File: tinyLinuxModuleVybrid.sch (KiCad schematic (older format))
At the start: 53 parts, among them M1 SCREW, M2 SCREW, M3 SCREW, M4 SCREW, M5 SCREW, M6 SCREW, M7 SCREW, M8 SCREW, Q1 2N7002BKT, Q2 2N7002BKT, Q3 2N7002BKT, X1 CONN_02x50, X10 MagJack100, X11 MICROSD, X12 CONN_01x03, X2 CONN_02x50, X3 USB4DUAL, X4 CONN_02x25, X5 ARM_JTAG_10, X6 USB4DUAL, X7 CONN_02x20, X8 CONN_02x14

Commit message: NEO_modifiziert
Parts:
- removed V1: 5V, Passives:V0805N, symbol V
- removed X12: CONN_01x03, Connector:PinHD-90-2.54-01x03-THT, symbol CONN_01X03
- removed X3, X6: USB4DUAL, Connector:USB4DUAL_A, symbol USB4DUAL
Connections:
- wire segments 429 -> 383
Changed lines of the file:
@@
 PTB5
-$Comp
-L GND #PWR062
-U 1 1 5601F6AC
-P 3900 4600
-F 0 "#PWR062" H 3900 4350 50  0001 C CNN
-F 1 "GND" H 3900 4450 50  0000 C CNN
-F 2 "" H 3900 4600 60  0000 C CNN
-F 3 "" H 3900 4600 60  0000 C CNN
-	1    3900 4600
-	1    0    0    -1
-$EndComp
 $Comp
 L GND #PWR063
@@
 $EndSheet
 $Comp
-L USB4DUAL X3
-U 1 1 56289EB9
-P 4550 2300
-F 0 "X3" H 4400 2900 50  0000 C CNN
-F 1 "USB4DUAL" V 4750 2350 50  0000 C CNN
-F 2 "Connector:USB4DUAL_A" H 4400 2550 60  0001 C CNN
-F 3 "" H 4400 2550 60  0000 C CNN
-	1    4550 2300
-	1    0    0    -1
-$EndComp
-$Comp
-L USB4DUAL X6
-U 1 1 56289FBC
-P 4550 3550
-F 0 "X6" H 4400 4150 50  0000 C CNN
-F 1 "USB4DUAL" V 4750 3600 50  0000 C CNN
-F 2 "Connector:USB4DUAL_A" H 4400 3800 60  0001 C CNN
-F 3 "" H 4400 3800 60  0000 C CNN
-	1    4550 3550
-	1    0    0    -1
-$EndComp
-$Comp
 L CONN_02X20 X7
 U 1 1 5628A750
@@
 USB
 $Comp
-L V V1
-U 1 1 56359904
-P 4100 4300
-F 0 "V1" V 4180 4300 50  0000 C CNN
-F 1 "5V" V 4020 4300 50  0000 C CNN
-F 2 "Passives:V0805N" V 4030 4300 30  0001 C CNN
-F 3 "" H 4100 4300 30  0000 C CNN
-	1    4100 4300
-	1    0    0    -1
-$EndComp
-$Comp
 L GND #PWR064
 U 1 1 56360C40
@@
 	2850 1600 5000 1600
 Wire Wire Line
-	3550 2600 2850 2600
-Wire Wire Line
-	2850 2500 3600 2500
-Wire Wire Line
-	3650 2400 2850 2400
-Wire Wire Line
-	2850 2300 3700 2300
-Connection ~ 3900 2600
-Wire Wire Line
-	4200 2100 3900 2100
-Connection ~ 3900 3350
-Wire Wire Line
-	4200 2600 3900 2600
-Connection ~ 3900 3850
-Wire Wire Line
-	3900 3350 4200 3350
-Connection ~ 3900 4550
-Wire Wire Line
-	3900 3850 4200 3850
-Wire Wire Line
-	3900 2100 3900 4600
-Wire Wire Line
-	4100 4550 3900 4550
-Wire Wire Line
-	4100 4500 4100 4550
-Connection ~ 4100 4050
-Wire Wire Line
-	4200 4050 4100 4050
-Wire Wire Line
-	4100 2800 4100 4100
-Wire Wire Line
-	4200 2800 4100 2800
-Connection ~ 4150 3050
-Wire Wire Line
-	4150 3550 4200 3550
-Connection ~ 4150 2300
-Wire Wire Line
-	4150 3050 4200 3050
-Connection ~ 4150 1800
-Wire Wire Line
-	4150 1800 4150 3550
-Wire Wire Line
-	4200 2300 4150 2300
-Wire Wire Line
 	1250 2700 600  2700
 Wire Wire Line
@@
 Wire Wire Line
 	2200 6800 2200 6750
-$Comp
-L CONN_01X03 X12
-U 1 1 563D7E2E
-P 8000 900
-F 0 "X12" H 8000 1100 50  0000 C CNN
-F 1 "CONN_01x03" V 8100 900 50  0000 C CNN
-F 2 "Connector:PinHD-90-2.54-01x03-THT" H 8000 900 60  0001 C CNN
-F 3 "" H 8000 900 60  0000 C CNN
-	1    8000 900
-	1    0    0    -1
-$EndComp
-Wire Wire Line
-	2850 800  7800 800
-Wire Wire Line
-	2850 900  7800 900
-$Comp
-L GND #PWR0100
-U 1 1 563D890F
-P 7750 1050
-F 0 "#PWR0100" H 7750 800 50  0001 C CNN
-F 1 "GND" H 7750 900 50  0000 C CNN
-F 2 "" H 7750 1050 60  0000 C CNN
-F 3 "" H 7750 1050 60  0000 C CNN
-	1    7750 1050
-	1    0    0    -1
-$EndComp
-Wire Wire Line
-	7800 1000 7750 1000
-Wire Wire Line
-	7750 1000 7750 1050
 $Comp
 L GND #PWR0101
@@
 	1    0    0    -1
 $EndComp
-Wire Wire Line
-	3700 2300 3700 3750
-Wire Wire Line
-	3650 3650 3650 2400
-Wire Wire Line
-	3600 2500 3600 3250
-Wire Wire Line
-	3550 3150 3550 2600
-Wire Wire Line
-	3750 2200 2850 2200
-Wire Wire Line
-	3750 1900 3750 2200
-Wire Wire Line
-	2850 2100 3700 2100
-Wire Wire Line
-	3700 2100 3700 2000
-Wire Wire Line
-	2850 2000 3400 2000
-Wire Wire Line
-	3400 2000 3400 2250
-Wire Wire Line
-	3400 2250 3750 2250
-Wire Wire Line
-	3750 2250 3750 2400
-Wire Wire Line
-	2850 1900 3500 1900
-Wire Wire Line
-	3500 1900 3500 2150
-Wire Wire Line
-	3500 2150 3800 2150
-Wire Wire Line
-	3800 2150 3800 2500
 $Comp
 L R R34
@@
 Wire Wire Line
 	3850 5200 3550 5200
-Wire Wire Line
-	3800 2500 4200 2500
-Wire Wire Line
-	3750 2400 4200 2400
-Wire Wire Line
-	4200 1900 3750 1900
-Wire Wire Line
-	3700 2000 4200 2000
-Wire Wire Line
-	3600 3250 4200 3250
-Wire Wire Line
-	3700 3750 4200 3750
-Wire Wire Line
-	4200 3650 3650 3650
-Wire Wire Line
-	4200 3150 3550 3150
 $Sheet
 S 8900 8150 1150 1450

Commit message: LAN Transformer footprint ergänzt
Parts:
- removed X10: MagJack100, Connector:MagJack100_Standard, symbol MagJack100
- added X?: LAN_Transformer, symbol LAN_Transformer
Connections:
- wire segments 383 -> 367
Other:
- note removed: "SCI3\n"
- moved on the sheet: C16, C17

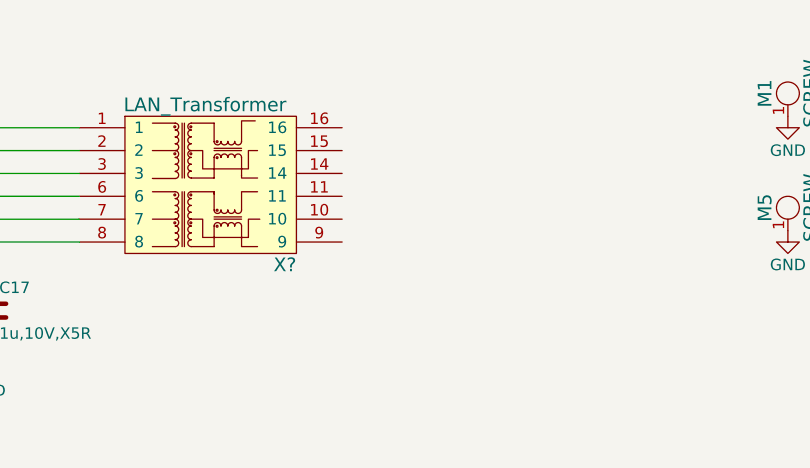
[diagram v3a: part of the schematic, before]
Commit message: NEO N8P durch M8N ersätzt
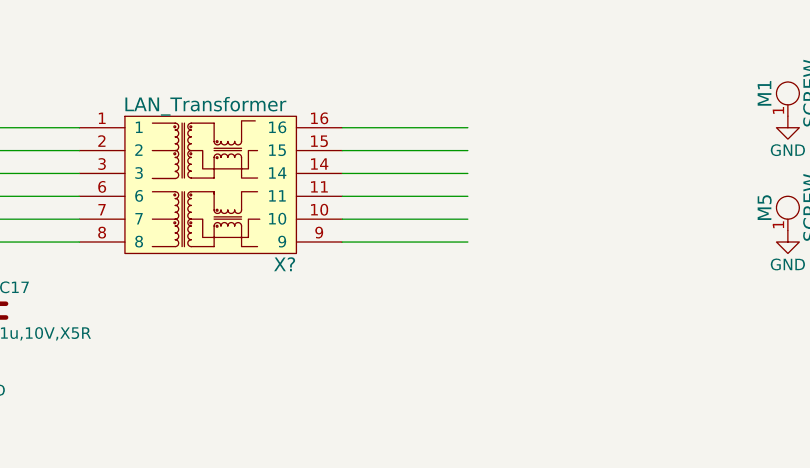
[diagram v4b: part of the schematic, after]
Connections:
- wire segments 367 -> 373
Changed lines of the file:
@@
 Wire Wire Line
 	2900 2850 3800 2850
+Wire Wire Line
+	6950 1100 7500 1100
+Wire Wire Line
+	6950 1200 7500 1200
+Wire Wire Line
+	6950 1300 7500 1300
+Wire Wire Line
+	6950 1400 7500 1400
+Wire Wire Line
+	6950 1500 7500 1500
+Wire Wire Line
+	6950 1600 7500 1600
 $EndSCHEMATC

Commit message: footprints ergänzt
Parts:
- removed R23, R24: 4.7k, Passives:R0402N, symbol R
- removed R34: 100k, Passives:R0402N, symbol R
- removed X4: CONN_02x25, symbol CONN_02x25
- removed X7: CONN_02x20, Connector:PinHD-2.54-02x20-THT, symbol CONN_02X20
- removed X8: CONN_02x14, Connector:PinHD-2.54-02x14-THT, symbol CONN_02X14
- X?: footprint (none) -> Communication:EDFP-J16
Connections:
- wire segments 373 -> 280

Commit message: added some footprints
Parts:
- removed M1, M2, M3, M4: SCREW, Mechanical:SCREW_M1.5, symbol SCREW
- removed X1, X2: CONN_02x50, Connector:Hirose-DF40-100DP, symbol CONN_02x50
- added X104: VybridBoard, myfootprint:VybridBoard, symbol VybridBoard
- gave numbers to parts that had none: 2
- renumbered C32 to C101, C33 to C102, C16 to C103, C17 to C104, FID1 to FID101, FID2 to FID102, FID3 to FID103, FID4 to FID104, LED1 to LED101, LED2 to LED102, LED3 to LED103, M5 to M102, M6 to M104, M7 to M106, M8 to M108, Q1 to Q101, Q2 to Q102, Q3 to Q103, R28 to R101, R8 to R102, R9 to R103, R10 to R104, R11 to R105, R35 to R106, R36 to R107, R37 to R108, R38 to R109, R25 to R110, R26 to R111, R27 to R112, R31 to R113, R32 to R114, R33 to R115, X11 to X101, X5 to X105
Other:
- moved on the sheet: X103

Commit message: added footprints
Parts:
- X102: footprint Communication:EDFP-J16 -> Communication:UL94-V0
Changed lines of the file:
@@
 F 0 "X102" H 6700 1000 60  0000 C CNN
 F 1 "LAN_Transformer" H 6350 1700 60  0000 C CNN
-F 2 "Communication:EDFP-J16" H 6270 1330 60  0001 C CNN
+F 2 "Communication:UL94-V0" H 6270 1330 60  0001 C CNN
 F 3 "" H 6270 1330 60  0000 C CNN
 	1    6400 1350

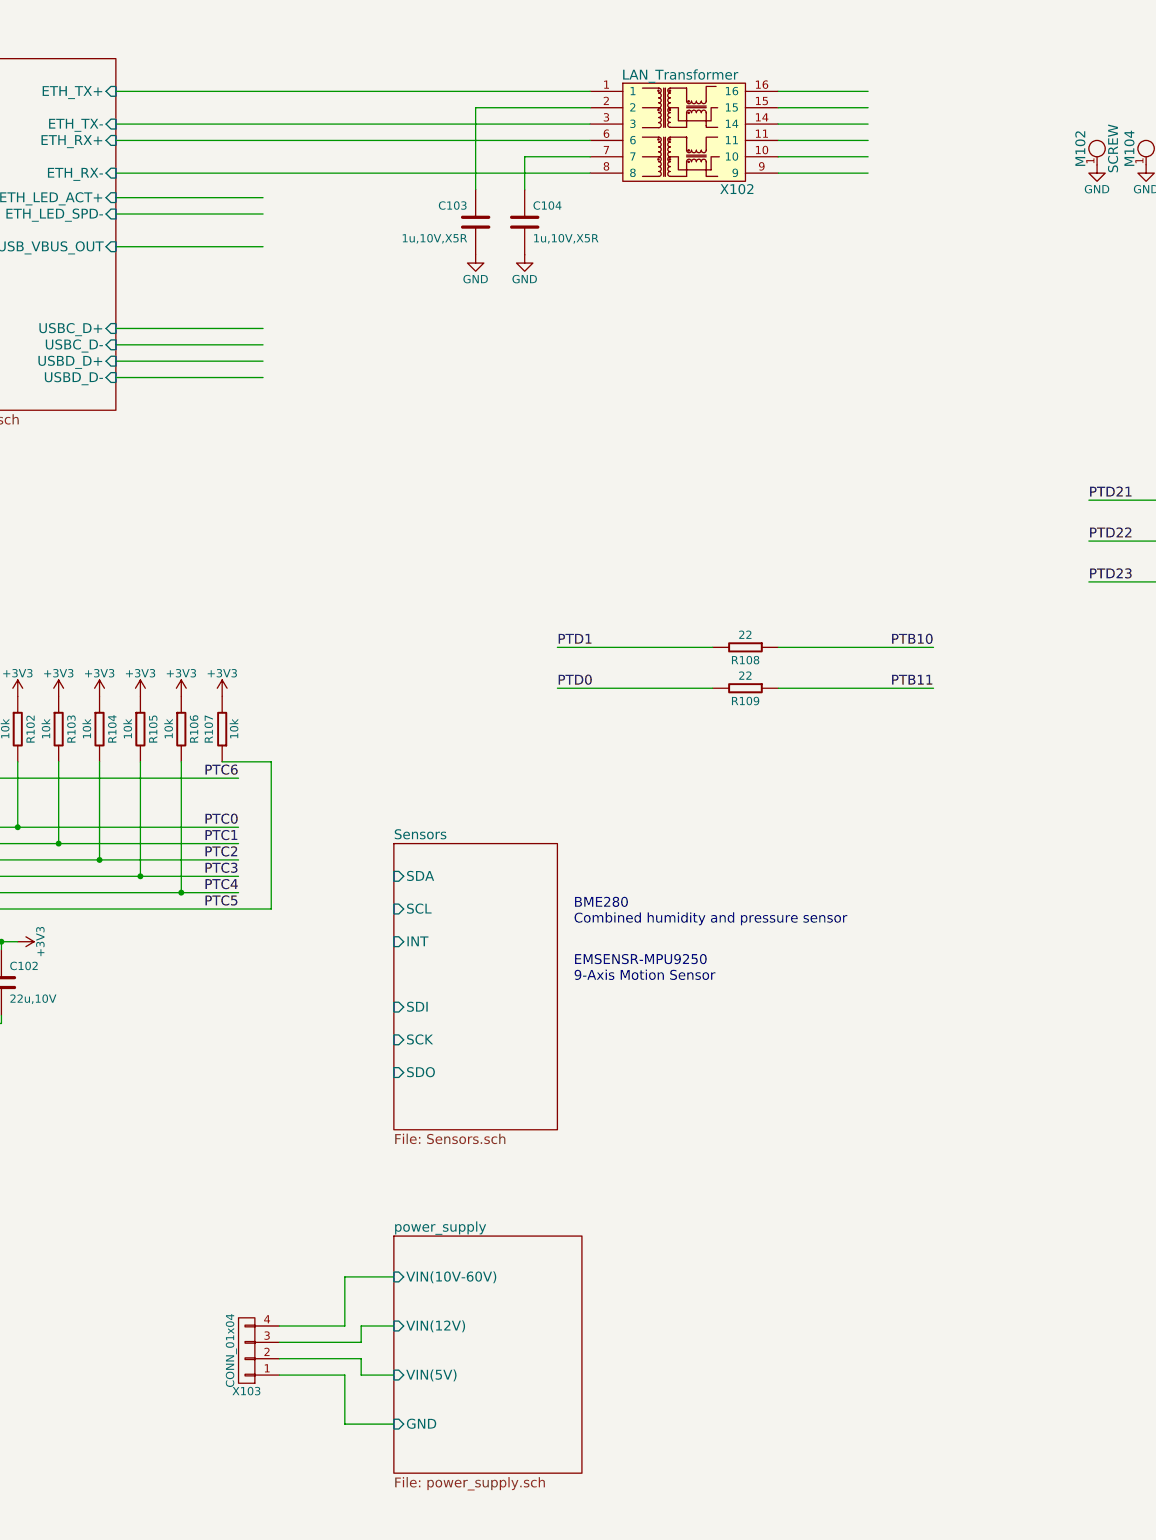
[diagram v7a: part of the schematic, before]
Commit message: adjusted power supply
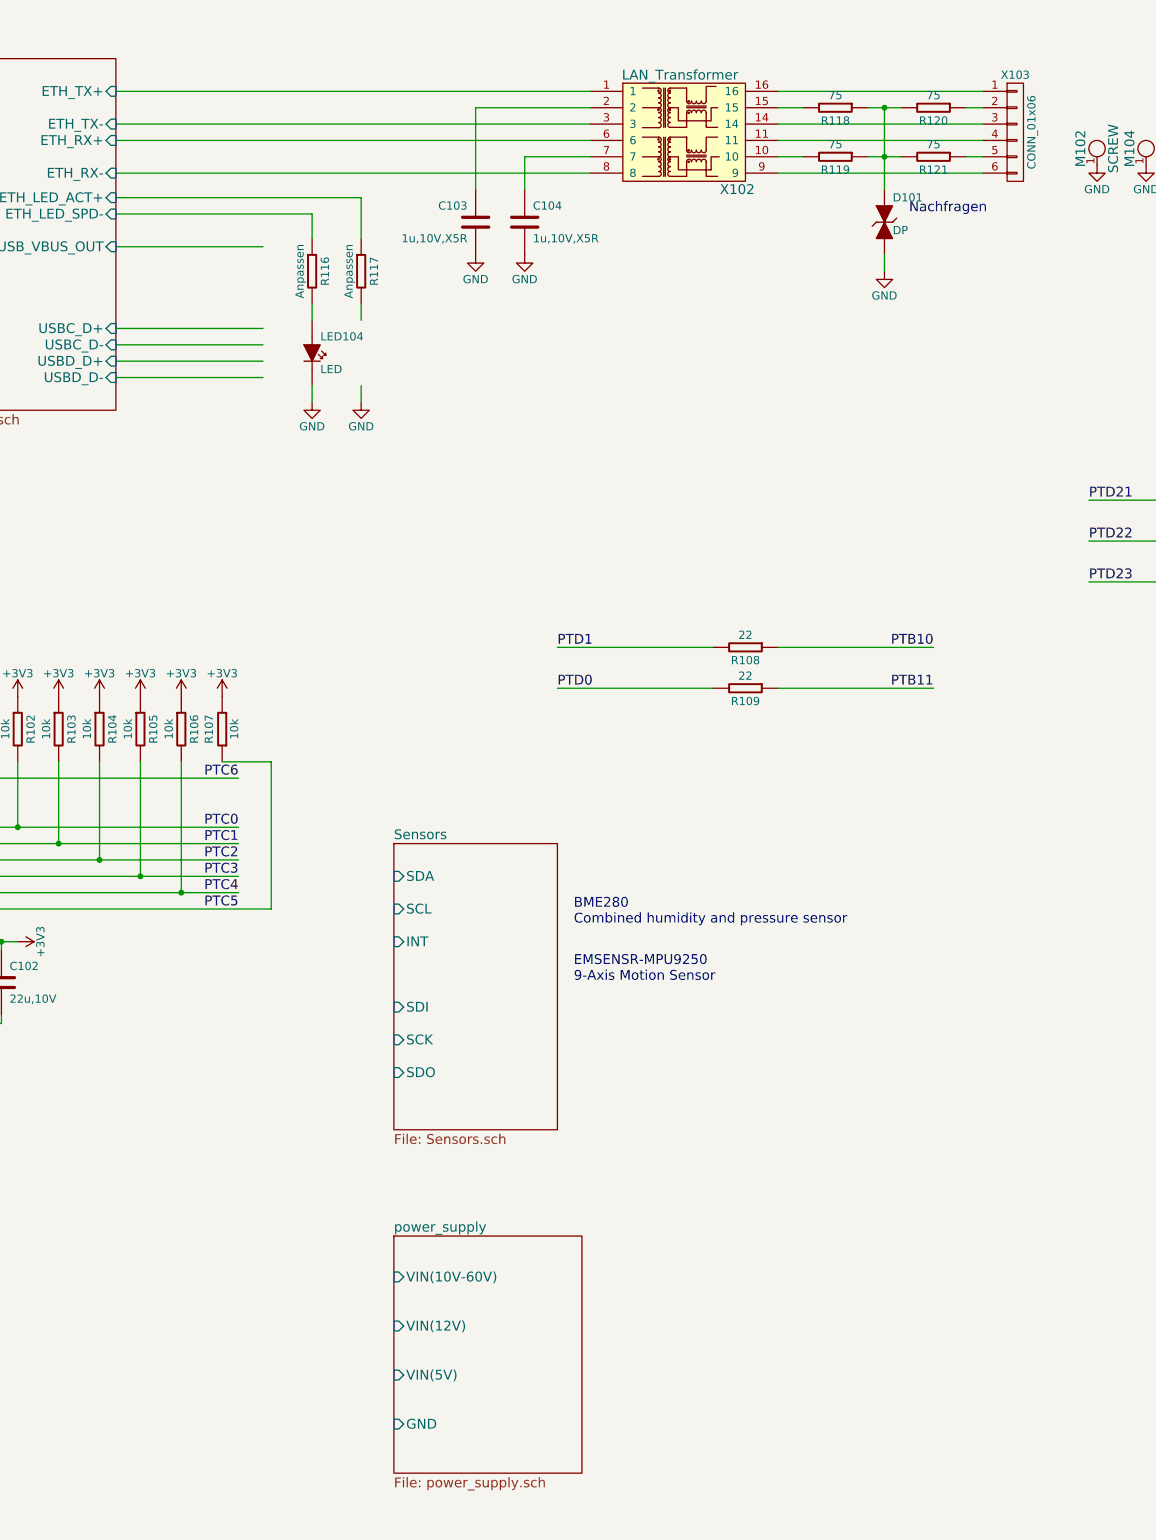
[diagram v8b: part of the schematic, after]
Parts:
- removed X103: CONN_01x04, Connector:MicroFit_43045-0409, symbol CONN_01x04
- added D101: DP, Passives:D_0402, symbol DP
- added LED104: LED, symbol LED
- added R116, R117: Anpassen, Passives:R0402N, symbol R
- added R118, R119, R120, R121: 75, Passives:R0402N, symbol R
- added X103: CONN_01x06, Connector:MLX127_53398_SMD-06, symbol CONN_01x06
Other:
- note added: "Nachfragen"
